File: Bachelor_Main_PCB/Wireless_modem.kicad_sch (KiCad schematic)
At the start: 54 parts, among them J10 JAE_SIM_Card_SF72S006, J12 M20-9990245, J18 CONMHF1-SMD-G-T, J19 CONMHF1-SMD-G-T, J20 CONMHF1-SMD-G-T, Q1 SSM3J358R,LF, Q10 NX3008NBKW, Q11 NX3008NBKW, Q5 NX3008NBKW, Q6 NX3008NBKW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

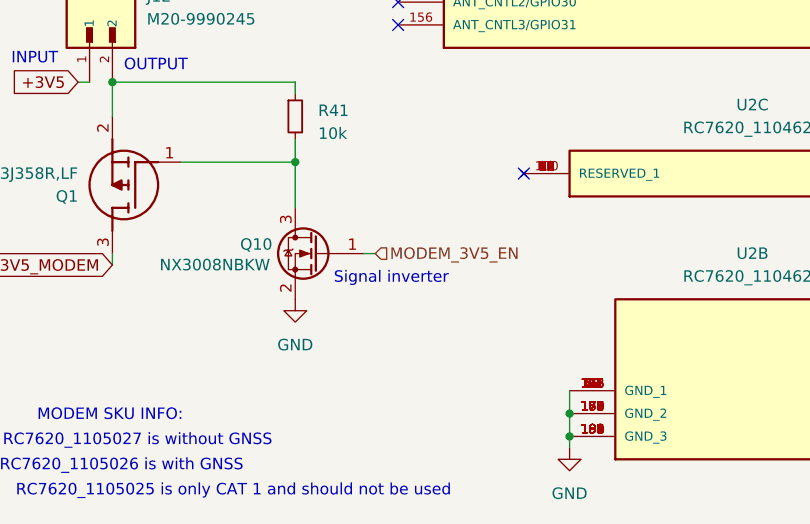
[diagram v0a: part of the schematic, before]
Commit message: Fixed schematic of SDcard enable pin
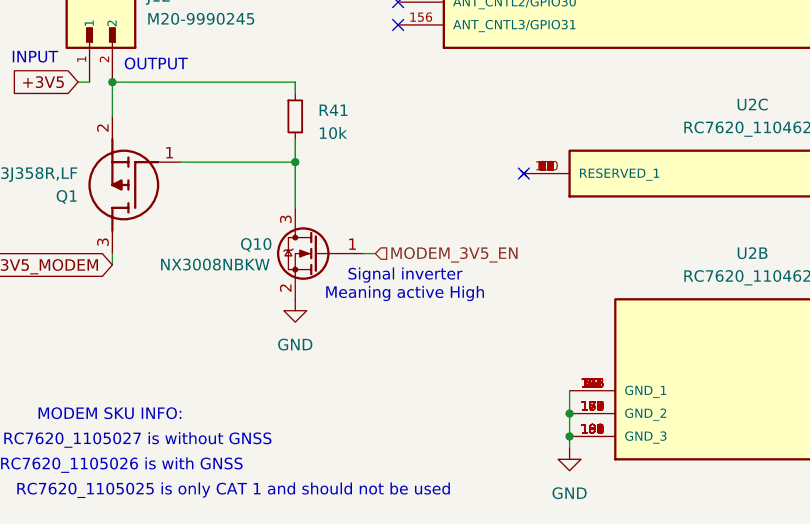
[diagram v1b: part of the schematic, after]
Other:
- note added: "Signal inverter Meaning active High"
- note removed: "Signal inverter"
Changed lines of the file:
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@@
 		)
 	)
-	(text "Signal inverter"
+	(text "Signal inverter\nMeaning active High"
 		(exclude_from_sim no)
-		(at 61.468 171.704 0)
+		(at 62.992 172.466 0)
 		(effects
 			(font

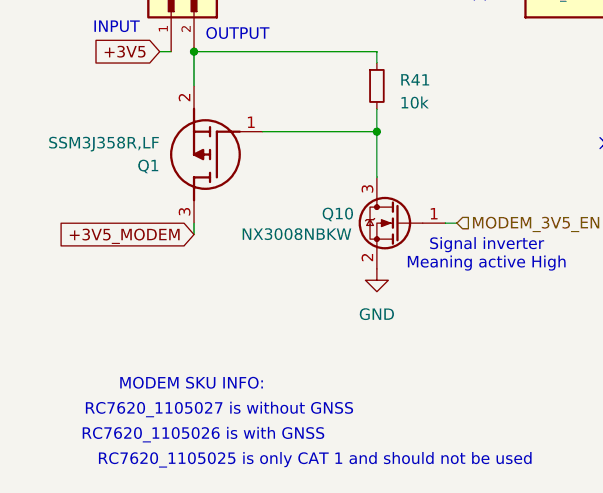
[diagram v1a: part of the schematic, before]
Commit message: add more LEDs
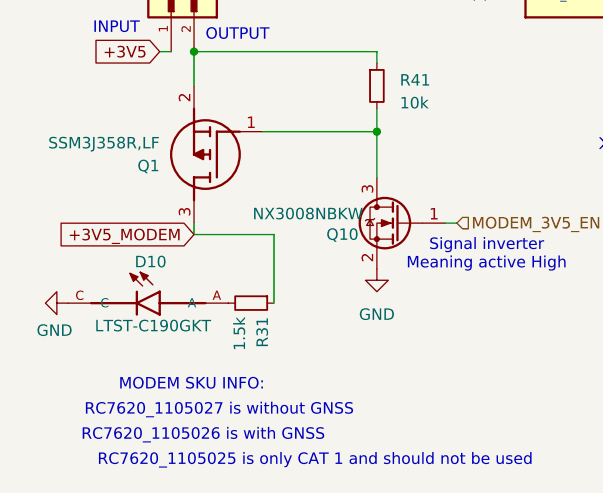
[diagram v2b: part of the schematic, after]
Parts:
- added D10: LTST-C190GKT, LTST-C190GKT:LEDM1608X80, symbol LTST-C190GKT:LTST-C190GKT
- added R31: 1.5k, Resistor_SMD:R_0402_1005Metric, symbol Device:R_Small
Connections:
- net +3V5_MODEM: now also R31.1
- net GND: now also D10.C
- new net: D10.A, R31.2

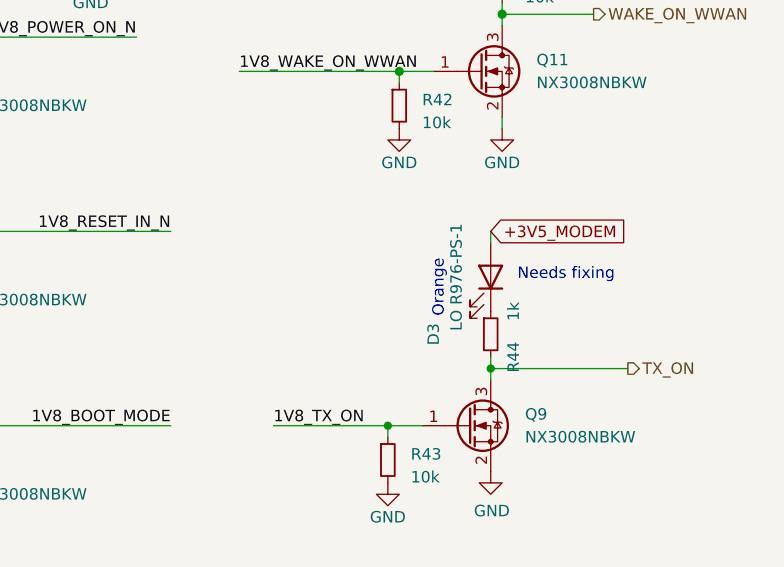
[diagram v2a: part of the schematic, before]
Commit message: Achematic review changes. Smal ones. Replaced TX_ON LED
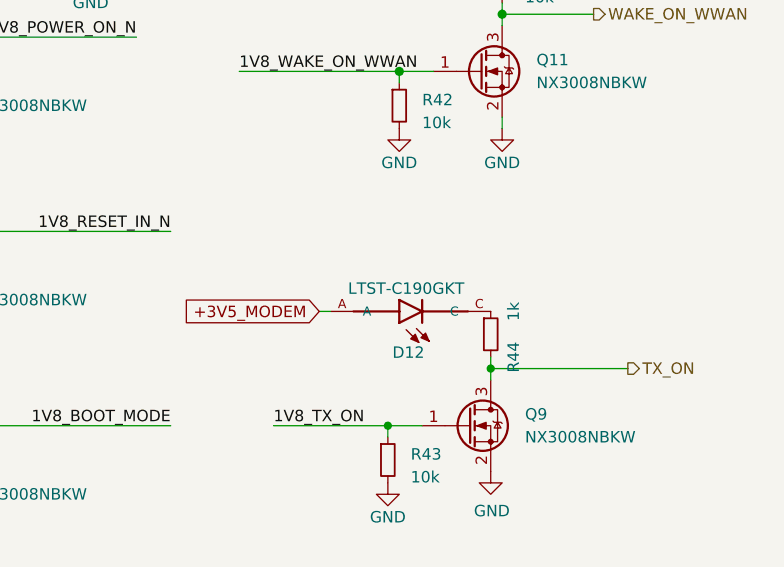
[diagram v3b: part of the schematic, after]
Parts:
- removed D3: LO R976-PS-1, jeffmakes-footprints:CHIPLED-0805, symbol Device:LED
- added D12: LTST-C190GKT, LTST-C190GKT:LEDM1608X80, symbol LTST-C190GKT:LTST-C190GKT
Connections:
- net +3V5_MODEM: now also D12.A
- net at R44.1: now also D12.C
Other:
- note removed: "Needs fixing"
- note removed: "Orange"
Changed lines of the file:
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@@
 		)
 	)
-	(text "Orange"
-		(exclude_from_sim no)
-		(at 248.92 132.715 90)
-		(effects
-			(font
-				(size 1.27 1.27)
-			)
-			(justify right bottom)
-		)
-	)
 	(text "Diversity \nantenna connector"
 		(exclude_from_sim no)
@@
 		)
 	)
-	(text "Needs fixing\n"
-		(exclude_from_sim no)
-		(at 262.382 134.366 0)
-		(effects
-			(font
-				(size 1.27 1.27)
-			)
-		)
-	)
 	(text "RC7620_1105026 is with GNSS"
 		(exclude_from_sim no)
@@
 	(wire
 		(pts
-			(xy 254 129.54) (xy 254 130.81)
-		)
-		(stroke
-			(width 0)
-			(type default)
-		)
-	)
-	(wire
-		(pts
 			(xy 219.71 64.77) (xy 212.09 64.77)
 		)
@@
 	(wire
 		(pts
+			(xy 234.95 138.43) (xy 236.22 138.43)
+		)
+		(stroke
+			(width 0)
+			(type default)
+		)
+	)
+	(wire
+		(pts
 			(xy 144.78 105.41) (xy 143.51 105.41)
 		)
@@
 	(global_label "+3V5_MODEM"
 		(shape input)
-		(at 254 129.54 0)
+		(at 234.95 138.43 180)
 		(fields_autoplaced yes)
 		(effects
@@
 				(size 1.27 1.27)
 			)
-			(justify left)
+			(justify right)
 		)
 		(property "Intersheetrefs" "${INTERSHEET_REFS}"
-			(at 269.6851 129.54 0)
+			(at 219.2649 138.43 0)
 			(effects
 				(font
 					(size 1.27 1.27)
 				)
-				(justify left)
+				(justify right)
 				(hide yes)
 			)
@@
 	)
 	(symbol
-		(lib_id "Device:LED")
-		(at 254 134.62 270)
-		(mirror x)
-		(unit 1)
-		(exclude_from_sim no)
-		(in_bom yes)
-		(on_board yes)
-		(dnp no)
-		(property "Reference" "D3"
-			(at 247.65 140.97 0)
-			(effects
-				(font
-					(size 1.27 1.27)
-				)
-			)
-		)
-		(property "Value" "LO R976-PS-1"
-			(at 250.19 134.62 0)
-			(effects
-				(font
-					(size 1.27 1.27)
-				)
-			)
-		)
-		(property "Footprint" "jeffmakes-footprints:CHIPLED-0805"
-			(at 254 134.62 0)
-			(effects
-				(font
-					(size 1.27 1.27)
-				)
-				(hide yes)
-			)
-		)
-		(property "Datasheet" "~"
-			(at 254 134.62 0)
-			(effects
-				(font
-					(size 1.27 1.27)
-				)
-				(hide yes)
-			)
-		)
-		(property "Description" ""
-			(at 254 134.62 0)
-			(effects
-				(font
-					(size 1.27 1.27)
-				)
-				(hide yes)
-			)
-		)
-		(property "Quantity" ""
-			(at 254 134.62 0)
-			(effects
-				(font
-					(size 1.27 1.27)
-				)
-				(hide yes)
-			)
-		)
-		(property "Digikey" "475-2488-6-ND"
-			(at 254 134.62 0)
-			(effects
-				(font
-					(size 1.27 1.27)
-				)
-				(hide yes)
-			)
-		)
-		(property "MPN" "LOR976-PS-1"
-			(at 254 134.62 0)
-			(effects
-				(font
-					(size 1.27 1.27)
-				)
-				(hide yes)
-			)
-		)
-		(property "Mouser" "720-LOR976-PS-1"
-			(at 254 134.62 0)
-			(effects
-				(font
-					(size 1.27 1.27)
-				)
-				(hide yes)
-			)
-		)
-		(property "Manufacturer" "Osram"
-			(at 254 134.62 0)
-			(effects
-				(font
-					(size 1.27 1.27)
-				)
-				(hide yes)
-			)
-		)
-		(property "Farnell" ""
-			(at 254 134.62 0)
-			(effects
-				(font
-					(size 1.27 1.27)
-				)
-				(hide yes)
-			)
-		)
-		(property "Field-1" ""
-			(at 254 134.62 0)
-			(effects
-				(font
-					(size 1.27 1.27)
-				)
-				(hide yes)
-			)
-		)
-		(property "Field4" ""
-			(at 254 134.62 0)
-			(effects
-				(font
-					(size 1.27 1.27)
-				)
-				(hide yes)
-			)
-		)
-		(property "Field5" ""
-			(at 254 134.62 0)
-			(effects
-				(font
-					(size 1.27 1.27)
-				)
-				(hide yes)
-			)
-		)
-		(property "MANUFACTURER" ""
-			(at 254 134.62 0)
-			(effects
-				(font
-					(size 1.27 1.27)
-				)
-				(hide yes)
-			)
-		)
-		(pin "1"
-		)
-		(pin "2"
-		)
-		(instances
-			(project "Bachelor_Main_PCB"
-				(path "/3544d663-329e-4884-b753-28436ca187e8/0bbef2a3-1d79-4cf0-b531-d6abf690b331"
-					(reference "D3")
-					(unit 1)
-				)
-			)
-		)
-	)
-	(symbol
 		(lib_id "power:GND")
 		(at 254 156.21 0)
@@
 					(unit 1)
 				)
+			)
+		)
+	)
+	(symbol
+		(lib_id "LTST-C190GKT:LTST-C190GKT")
+		(at 246.38 138.43 180)
+		(unit 1)
+		(exclude_from_sim no)
+		(in_bom yes)
+		(on_board yes)
+		(dnp no)
+		(property "Reference" "D12"
+			(at 244.856 143.002 0)
+			(effects
+				(font
+					(size 1.27 1.27)
+				)
+			)
+		)
+		(property "Value" "LTST-C190GKT"
+			(at 244.602 135.89 0)
+			(effects
+				(font
+					(size 1.27 1.27)
+				)
+			)
+		)
+		(property "Footprint" "LTST-C190GKT:LEDM1608X80"
+			(at 246.38 138.43 0)
+			(effects
+				(font
+					(size 1.27 1.27)
+				)
+				(justify bottom)
+				(hide yes)
+			)
+		)
+		(property "Datasheet" ""
+			(at 246.38 138.43 0)
+			(effects
+				(font
+					(size 1.27 1.27)
+				)
+				(hide yes)
+			)
+		)
+		(property "Description" ""
+			(at 246.38 138.43 0)
+			(effects
+				(font
+					(size 1.27 1.27)
+				)
+				(hide yes)
+			)
+		)
+		(property "MF" "Lite-On Inc."
+			(at 246.38 138.43 0)
+			(effects
+				(font
+					(size 1.27 1.27)
+				)
+				(justify bottom)
+				(hide yes)
+			)
+		)
+		(property "Description_1" "Green 569nm LED Indication - Discrete 2.1V 0603 (1608 Metric)"
+			(at 246.38 138.43 0)
+			(effects
+				(font
+					(size 1.27 1.27)
+				)
+				(justify bottom)
+				(hide yes)
+			)
+		)
+		(property "Package" "0603 Lite-On"
+			(at 246.38 138.43 0)
+			(effects
+				(font
+					(size 1.27 1.27)
+				)
+				(justify bottom)
+				(hide yes)
+			)
+		)
+		(property "Price" "None"
+			(at 246.38 138.43 0)
+			(effects
+				(font
+					(size 1.27 1.27)
+				)
+				(justify bottom)
+				(hide yes)
+			)
+		)
+		(property "Check_prices" "https://www.snapeda.com/parts/LTST-C190GKT/Lite-On/view-part/?ref=eda"
+			(at 246.38 138.43 0)
+			(effects
+				(font
+					(size 1.27 1.27)
+				)
+				(justify bottom)
+				(hide yes)
+			)
+		)
+		(property "SnapEDA_Link" "https://www.snapeda.com/parts/LTST-C190GKT/Lite-On/view-part/?ref=snap"
+			(at 246.38 138.43 0)
+			(effects
+				(font
+					(size 1.27 1.27)
+				)
+				(justify bottom)
+				(hide yes)
+			)
+		)
+		(property "MP" "LTST-C190GKT"
+			(at 246.38 138.43 0)
+			(effects
+				(font
+					(size 1.27 1.27)
+				)
+				(justify bottom)
+				(hide yes)
+			)
+		)
+		(property "Availability" "In Stock"
+			(at 246.38 138.43 0)
+			(effects
+				(font
+					(size 1.27 1.27)
+				)
+				(justify bottom)
+				(hide yes)
+			)
+		)
+		(property "MANUFACTURER" "Lite On"
+			(at 246.38 138.43 0)
+			(effects
+				(font
+					(size 1.27 1.27)
+				)
+				(justify bottom)
+				(hide yes)
+			)
+		)
+		(pin "A"
+		)
+		(pin "C"
+		)
+		(instances
+			(project "Bachelor_Main_PCB"
+				(path "/3544d663-329e-4884-b753-28436ca187e8/0bbef2a3-1d79-4cf0-b531-d6abf690b331"
+					(reference "D12")
+					(unit 1)
+				)

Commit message: Add correct 47uF partno and footpring
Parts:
- C31, C32: footprint Capacitor_SMD:C_0603_1608Metric -> Capacitor_SMD:C_1206_3216Metric; Part-no (none) -> GRM31CR61A476ME15L; Voltage rating (none) -> 10v
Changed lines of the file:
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@@
 			)
 		)
-		(property "Footprint" "Capacitor_SMD:C_0603_1608Metric"
+		(property "Footprint" "Capacitor_SMD:C_1206_3216Metric"
 			(at 143.51 179.07 0)
 			(effects
@@
 			)
 		)
+		(property "Part-no" "GRM31CR61A476ME15L "
+			(at 147.574 179.07 0)
+			(effects
+				(font
+					(size 1.27 1.27)
+				)
+				(hide yes)
+			)
+		)
+		(property "Voltage rating" "10v"
+			(at 143.51 179.07 0)
+			(effects
+				(font
+					(size 1.27 1.27)
+				)
+				(hide yes)
+			)
+		)
 		(pin "2"
 		)
@@
 			)
 		)
-		(property "Footprint" "Capacitor_SMD:C_0603_1608Metric"
+		(property "Footprint" "Capacitor_SMD:C_1206_3216Metric"
 			(at 135.89 179.07 0)
 			(effects
@@
 			(at 135.89 179.07 0)
 			(effects
+				(font
+					(size 1.27 1.27)
+				)
+				(hide yes)
+			)
+		)
+		(property "Part-no" "GRM31CR61A476ME15L "
+			(at 137.668 179.07 0)
+			(effects
+				(font
+					(size 1.27 1.27)
+				)
+				(hide yes)
+			)
+		)
+		(property "Voltage rating" "10v"
+			(at 135.89 179.07 0)
+			(effects

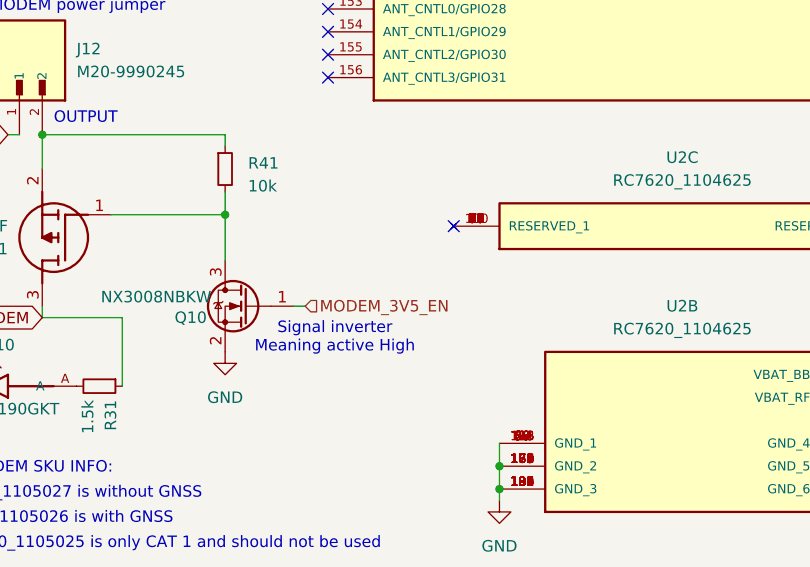
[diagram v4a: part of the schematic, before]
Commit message: Add signal inverter to RPIcm enable pin.
In order to protect MCU against 5v input on GPIO pin.
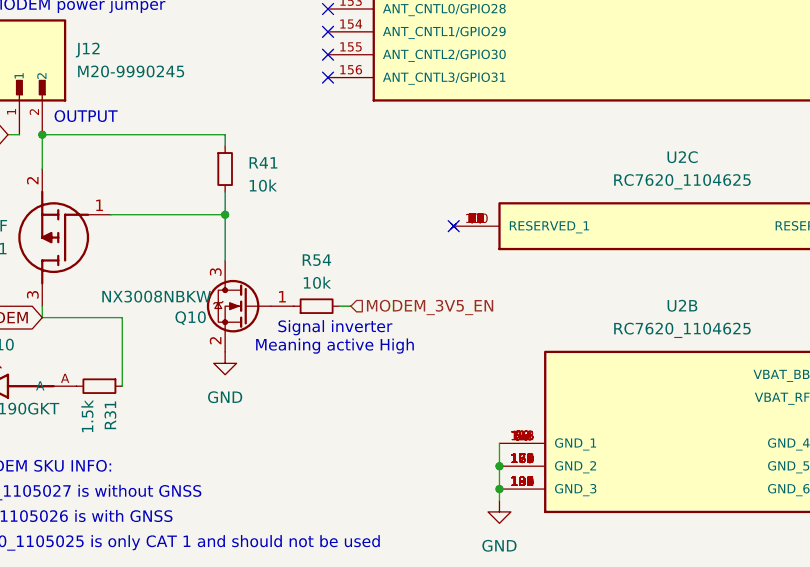
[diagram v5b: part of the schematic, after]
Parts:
- added R54: 10k, Resistor_SMD:R_0402_1005Metric, symbol Device:R_Small
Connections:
- net MODEM_3V5_EN: now also R54.2; no longer Q10.1 (G)
- new net: Q10.1 (G), R54.1
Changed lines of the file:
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@@
 	(wire
 		(pts
+			(xy 63.5 168.91) (xy 64.77 168.91)
+		)
+		(stroke
+			(width 0)
+			(type default)
+		)
+	)
+	(wire
+		(pts
 			(xy 212.09 54.61) (xy 212.09 64.77)
 		)
@@
 	(wire
 		(pts
-			(xy 58.42 168.91) (xy 59.69 168.91)
-		)
-		(stroke
-			(width 0)
-			(type default)
-		)
-	)
-	(wire
-		(pts
 			(xy 144.78 125.73) (xy 143.51 125.73)
 		)
@@
 	(hierarchical_label "MODEM_3V5_EN"
 		(shape input)
-		(at 59.69 168.91 0)
+		(at 64.77 168.91 0)
 		(effects
 			(font
@@
 				)
 			)
+		)
+	)
+	(symbol
+		(lib_id "Device:R_Small")
+		(at 60.96 168.91 90)
+		(unit 1)
+		(exclude_from_sim no)
+		(in_bom yes)
+		(on_board yes)
+		(dnp no)
+		(fields_autoplaced yes)
+		(property "Reference" "R54"
+			(at 60.96 163.83 90)
+			(effects
+				(font
+					(size 1.27 1.27)
+				)
+			)
+		)
+		(property "Value" "10k"
+			(at 60.96 166.37 90)
+			(effects
+				(font
+					(size 1.27 1.27)
+				)
+			)
+		)
+		(property "Footprint" "Resistor_SMD:R_0402_1005Metric"
+			(at 60.96 168.91 0)
+			(effects
+				(font
+					(size 1.27 1.27)
+				)
+				(hide yes)
+			)
+		)
+		(property "Datasheet" "~"
+			(at 60.96 168.91 0)
+			(effects
+				(font
+					(size 1.27 1.27)
+				)
+				(hide yes)
+			)
+		)
+		(property "Description" ""
+			(at 60.96 168.91 0)
+			(effects
+				(font
+					(size 1.27 1.27)
+				)
+				(hide yes)
+			)
+		)
+		(property "Quantity" ""
+			(at 60.96 168.91 0)
+			(effects
+				(font
+					(size 1.27 1.27)
+				)
+				(hide yes)
+			)
+		)
+		(property "Digikey" ""
+			(at 60.96 168.91 0)
+			(effects
+				(font
+					(size 1.27 1.27)
+				)
+				(hide yes)
+			)
+		)
+		(property "MPN" ""
+			(at 60.96 168.91 0)
+			(effects
+				(font
+					(size 1.27 1.27)
+				)
+				(hide yes)
+			)
+		)
+		(property "Mouser" ""
+			(at 60.96 168.91 0)
+			(effects
+				(font
+					(size 1.27 1.27)
+				)
+				(hide yes)
+			)
+		)
+		(property "Farnell" ""
+			(at 60.96 168.91 0)
+			(effects
+				(font
+					(size 1.27 1.27)
+				)
+				(hide yes)
+			)
+		)
+		(property "Field-1" ""
+			(at 60.96 168.91 0)
+			(effects
+				(font
+					(size 1.27 1.27)
+				)
+				(hide yes)
+			)
+		)
+		(property "Field4" ""
+			(at 60.96 168.91 0)
+			(effects
+				(font
+					(size 1.27 1.27)
+				)
+				(hide yes)
+			)
+		)
+		(property "Field5" ""
+			(at 60.96 168.91 0)
+			(effects
+				(font
+					(size 1.27 1.27)
+				)
+				(hide yes)
+			)
+		)
+		(property "MANUFACTURER" ""
+			(at 60.96 168.91 0)
+			(effects
+				(font
+					(size 1.27 1.27)
+				)
+				(hide yes)
+			)
+		)
+		(pin "1"
+		)
+		(pin "2"
+		)
+		(instances
+			(project "Bachelor_Main_PCB"
+				(path "/3544d663-329e-4884-b753-28436ca187e8/0bbef2a3-1d79-4cf0-b531-d6abf690b331"
+					(reference "R54")
+					(unit 1)
+				)
+			)
